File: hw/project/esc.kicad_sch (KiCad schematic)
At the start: 0 parts

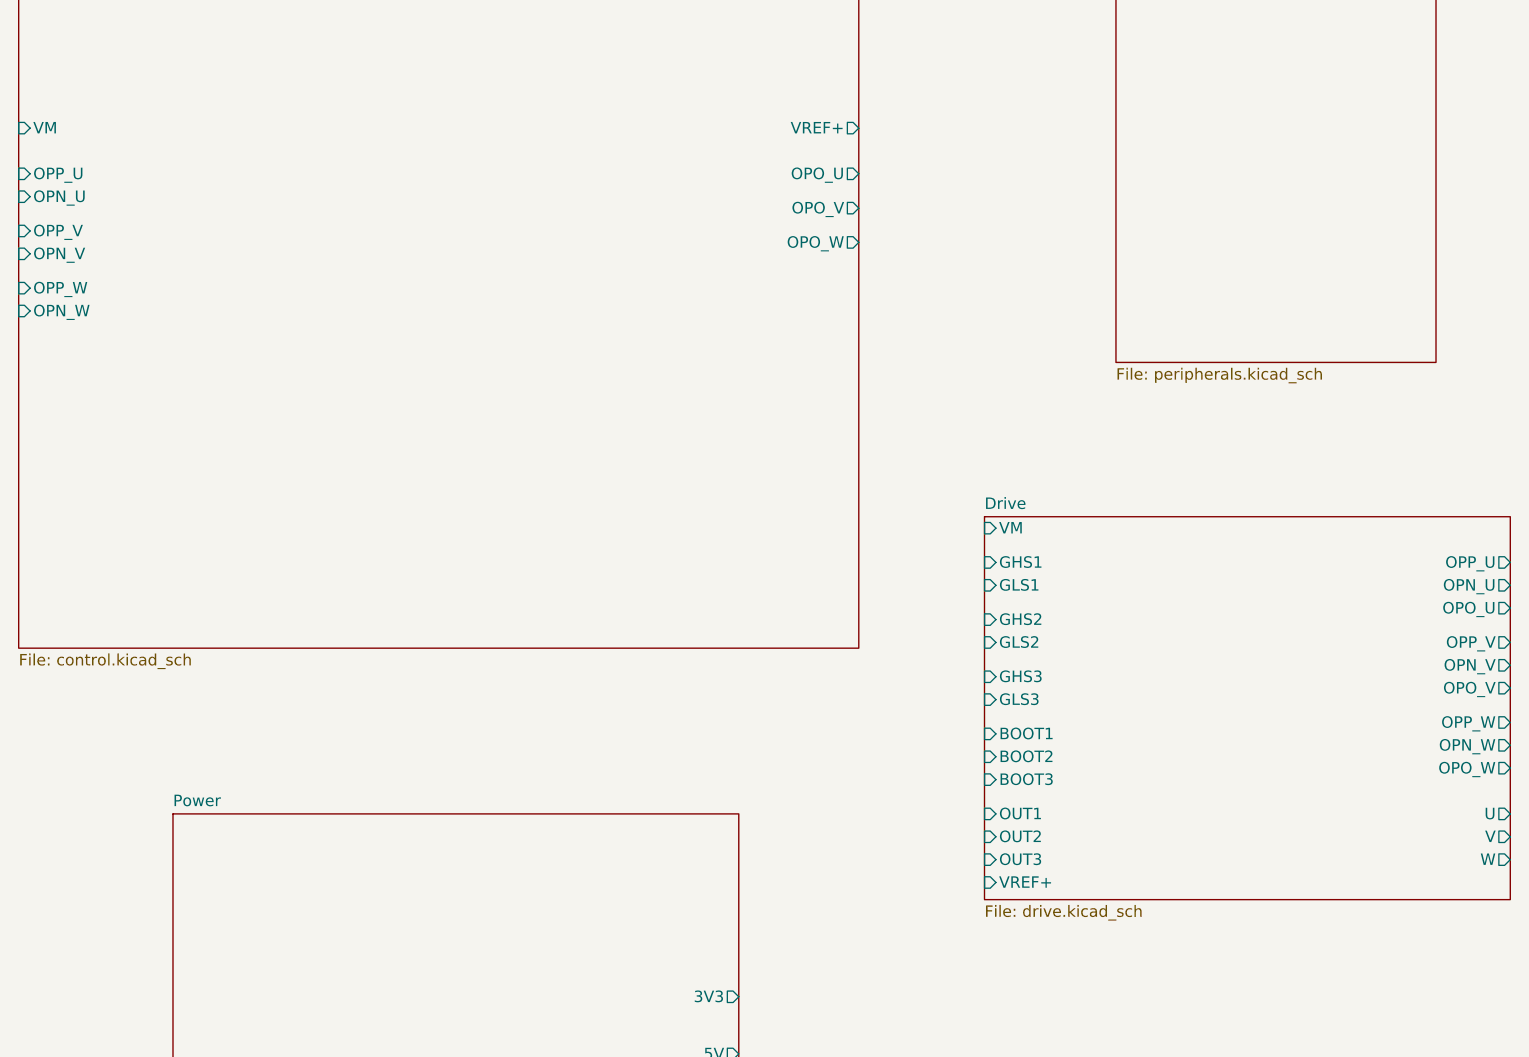
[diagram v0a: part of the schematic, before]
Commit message: Remove VINP and VOUT pins, updated pin functions on VINM pins
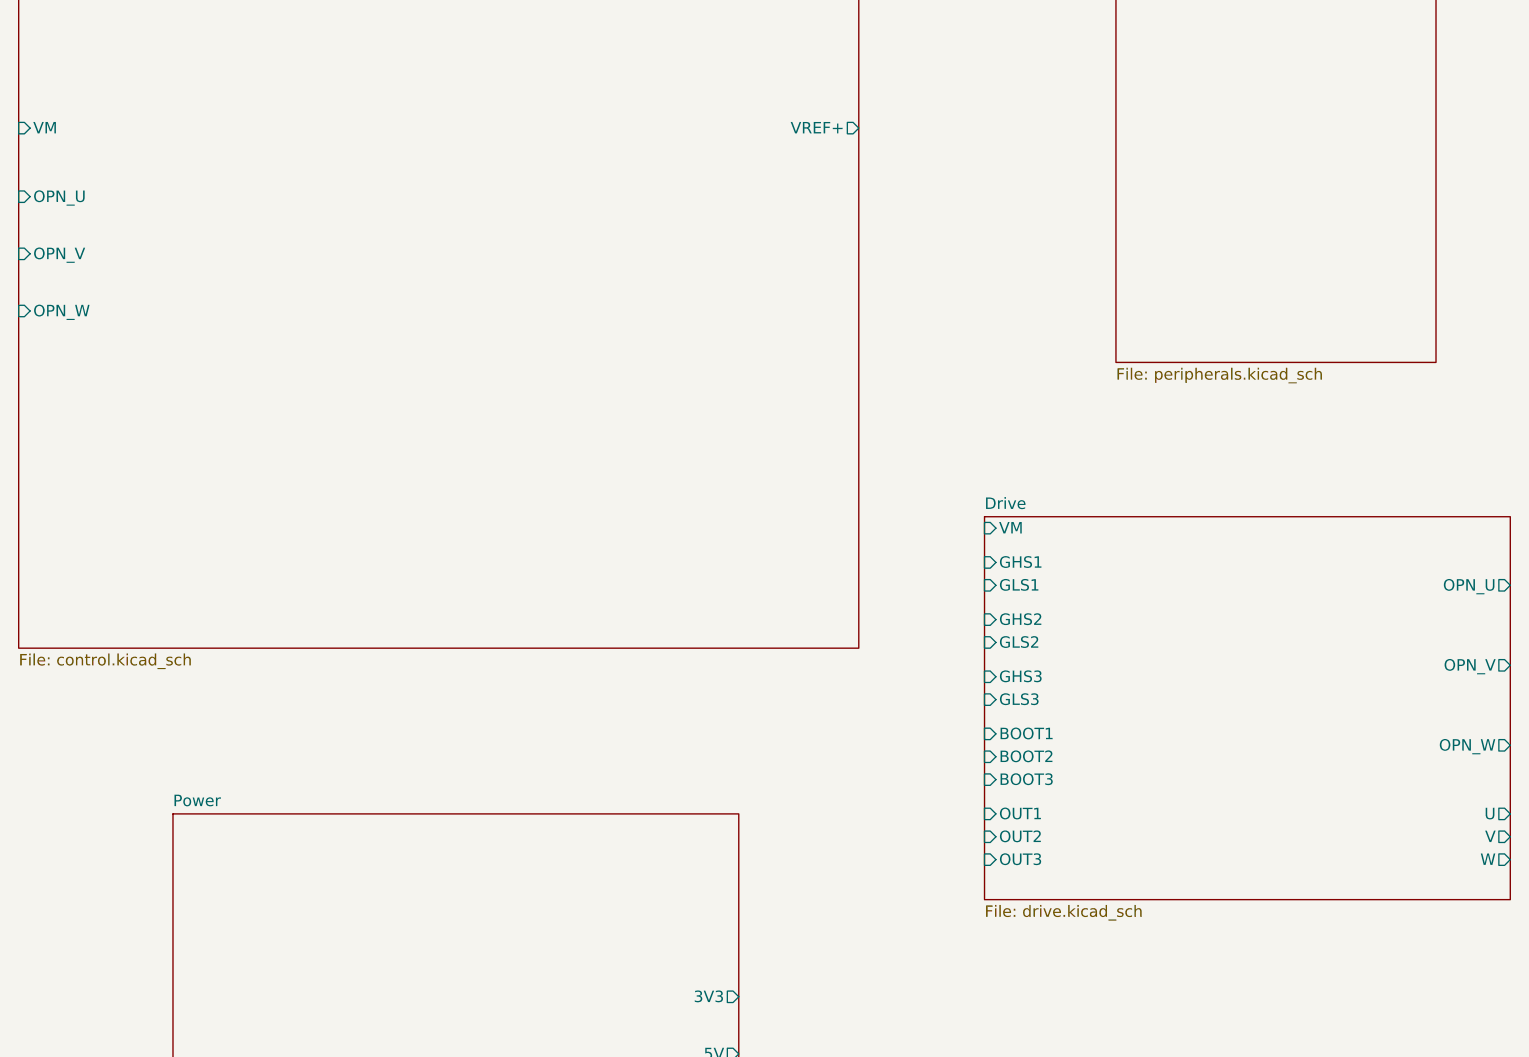
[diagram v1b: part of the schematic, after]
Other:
- sheet Control ports: added none; removed OPO_U, OPO_V, OPO_W, OPP_U, OPP_V, OPP_W
- sheet Drive ports: added none; removed OPO_U, OPO_V, OPO_W, OPP_U, OPP_V, OPP_W, VREF+
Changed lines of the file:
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@@
-			)
-		)
-		(pin "OPO_U" output
-			(at 106.68 44.45 0)
-			(effects
-				(font
-					(size 1.27 1.27)
-				)
-				(justify right)
-			)
-		)
-		(pin "OPO_V" output
-			(at 106.68 48.26 0)
-			(effects
-				(font
-					(size 1.27 1.27)
-				)
-				(justify right)
-			)
-		)
-		(pin "OPO_W" output
-			(at 106.68 52.07 0)
-			(effects
-				(font
-					(size 1.27 1.27)
-				)
-				(justify right)
-			)
-		)
-		(pin "OPP_U" input
-			(at 13.335 44.45 180)
-			(effects
-				(font
-					(size 1.27 1.27)
-				)
-				(justify left)
-			)
-		)
-		(pin "OPP_V" input
-			(at 13.335 50.8 180)
-			(effects
-				(font
-					(size 1.27 1.27)
-				)
-				(justify left)
-			)
-		)
-		(pin "OPP_W" input
-			(at 13.335 57.15 180)
-			(effects
-				(font
-					(size 1.27 1.27)
-				)
-				(justify left)
 			)
 		)
@@
 			)
 		)
-		(pin "VREF+" input
-			(at 120.65 123.19 180)
-			(effects
-				(font
-					(size 1.27 1.27)
-				)
-				(justify left)
-			)
-		)
-		(pin "OPP_V" output
-			(at 179.07 96.52 0)
-			(effects
-				(font
-					(size 1.27 1.27)
-				)
-				(justify right)
-			)
-		)
-		(pin "OPO_W" output
-			(at 179.07 110.49 0)
-			(effects
-				(font
-					(size 1.27 1.27)
-				)
-				(justify right)
-			)
-		)
-		(pin "OPP_U" output
-			(at 179.07 87.63 0)
-			(effects
-				(font
-					(size 1.27 1.27)
-				)
-				(justify right)
-			)
-		)
 		(pin "OPN_U" output
 			(at 179.07 90.17 0)
@@
 			)
 		)
-		(pin "OPP_W" output
-			(at 179.07 105.41 0)
-			(effects
-				(font
-					(size 1.27 1.27)
-				)
-				(justify right)
-			)
-		)
 		(pin "OPN_W" output
 			(at 179.07 107.95 0)
@@
 			)
 		)
-		(pin "OPO_V" output
-			(at 179.07 101.6 0)
-			(effects
-				(font
-					(size 1.27 1.27)
-				)
-				(justify right)
-			)
-		)
 		(pin "OPN_V" output
 			(at 179.07 99.06 0)
 			(effects
 				(font
-					(size 1.27 1.27)
-				)
-				(justify right)
-			)
-		)
-		(pin "OPO_U" output
-			(at 179.07 92.71 0)
-			(effects
-				(font

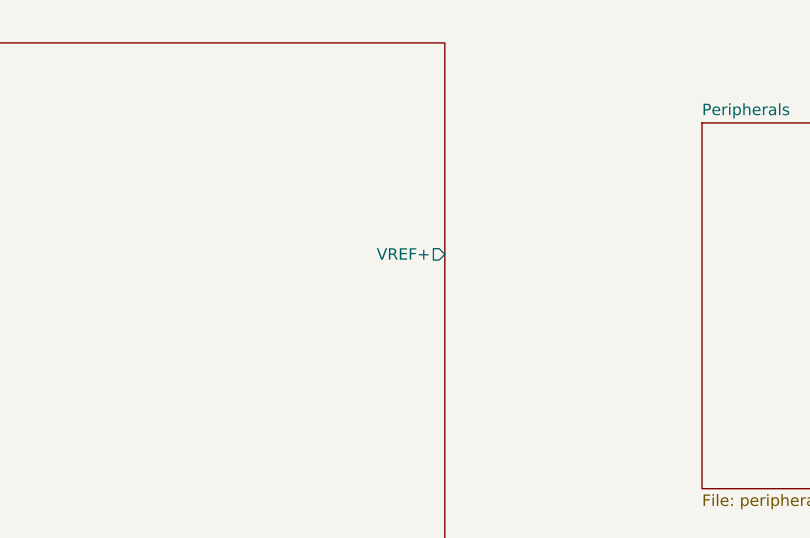
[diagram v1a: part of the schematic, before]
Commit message: Remove VREF+ as hierarchical label cuz PGA used now
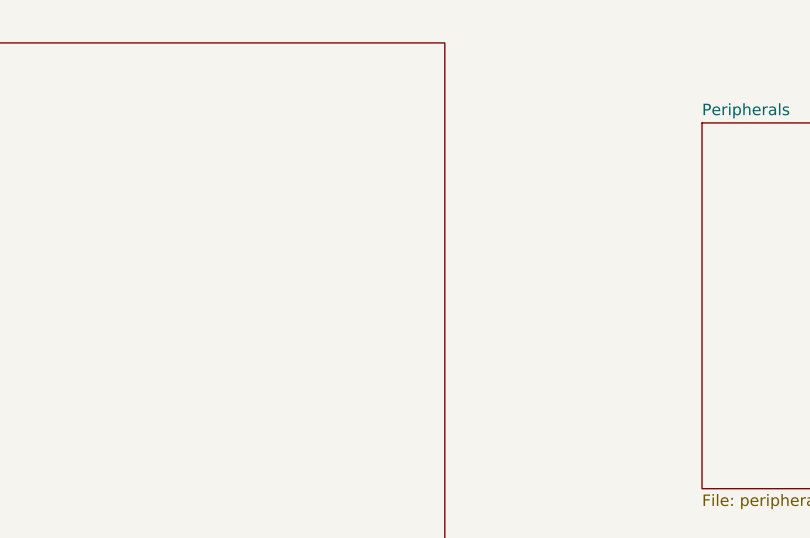
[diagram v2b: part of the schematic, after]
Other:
- sheet Control ports: added none; removed VREF+
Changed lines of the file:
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@@
-			)
-		)
-		(pin "VREF+" output
-			(at 106.68 39.37 0)
-			(effects
-				(font
-					(size 1.27 1.27)
-				)
-				(justify right)
 			)
 		)

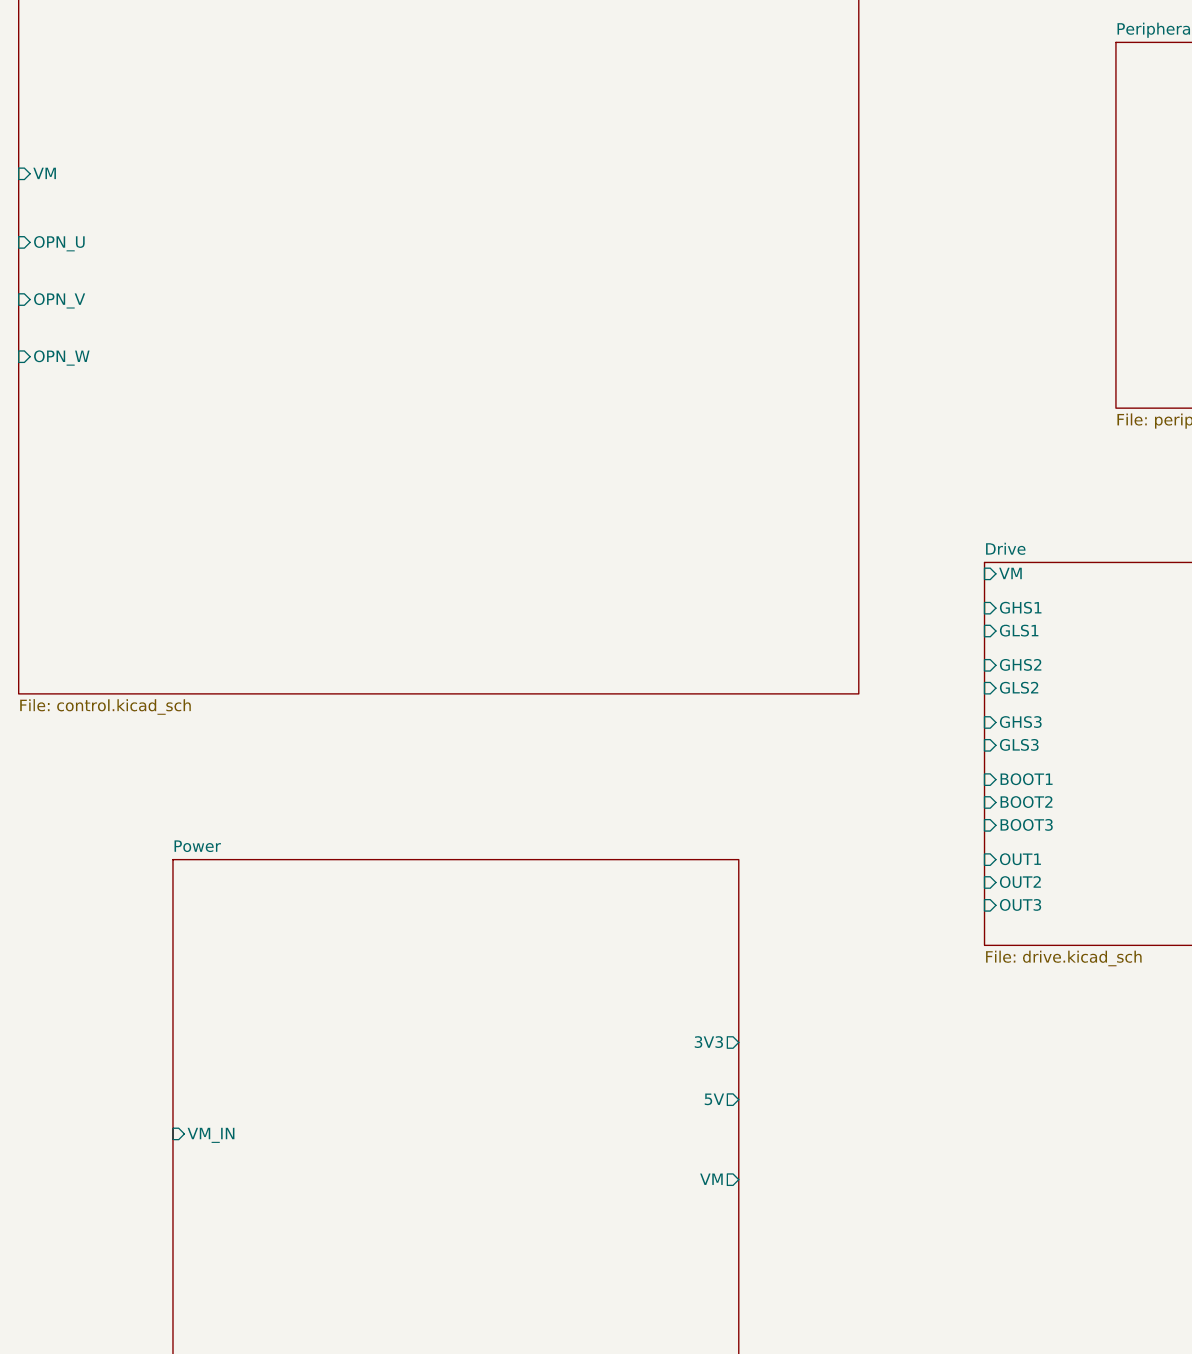
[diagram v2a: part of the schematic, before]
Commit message: Change VM to global source
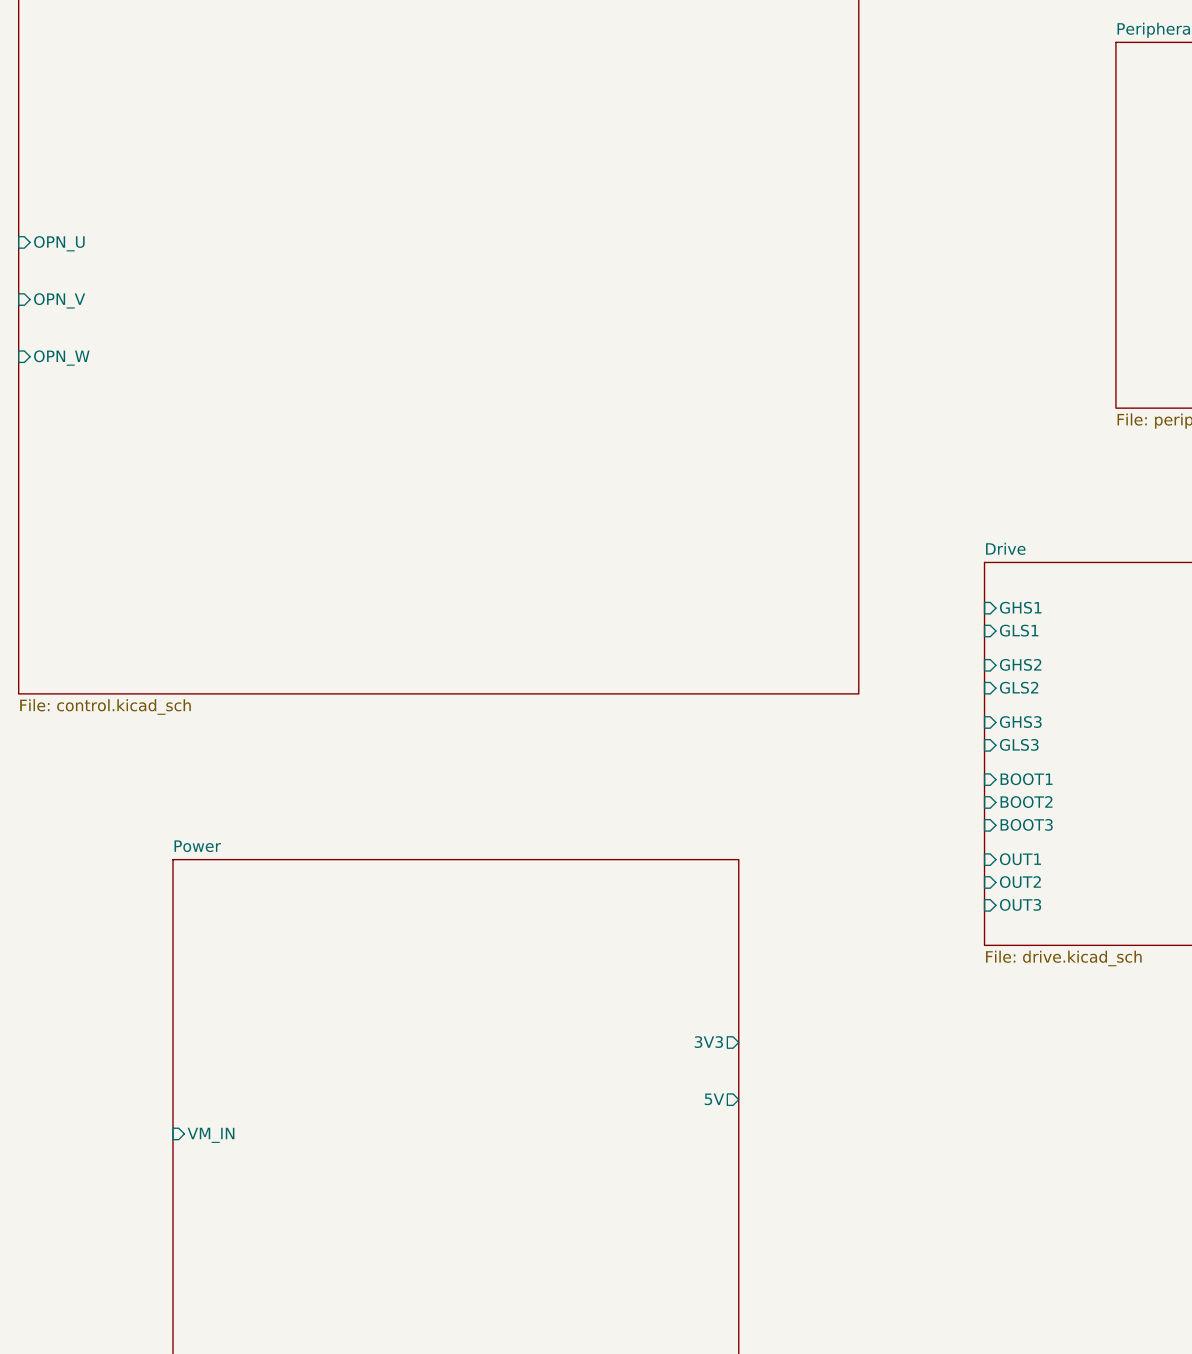
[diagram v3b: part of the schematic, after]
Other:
- sheet Control ports: added none; removed VM
- sheet Drive ports: added none; removed VM
- sheet Power ports: added none; removed VM
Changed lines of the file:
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@@
-			)
-		)
-		(pin "VM" input
-			(at 13.335 39.37 180)
-			(effects
-				(font
-					(size 1.27 1.27)
-				)
-				(justify left)
 			)
 		)
@@
 			)
 		)
-		(pin "VM" output
-			(at 93.345 151.13 0)
-			(effects
-				(font
-					(size 1.27 1.27)
-				)
-				(justify right)
-			)
-		)
 		(pin "VM_IN" input
 			(at 30.48 146.05 180)
@@
 			(effects
 				(font
-					(size 1.27 1.27)
-				)
-				(justify left)
-			)
-		)
-		(pin "VM" input
-			(at 120.65 83.82 180)
-			(effects
-				(font

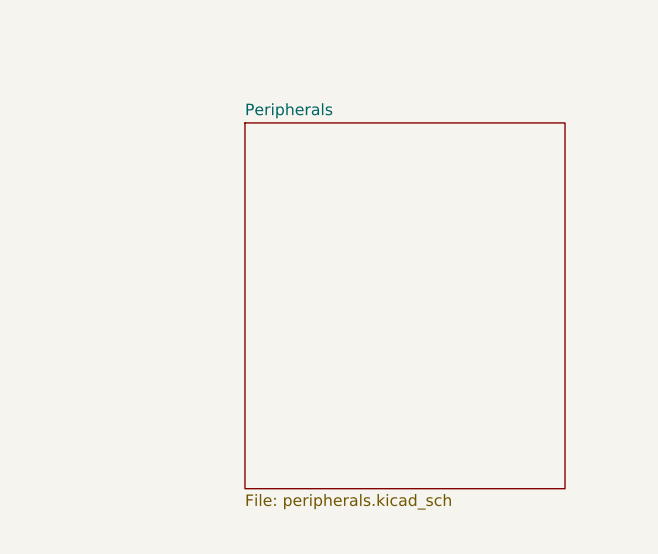
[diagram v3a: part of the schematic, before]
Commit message: Update root sheet with periph H labels, excluding LED signals
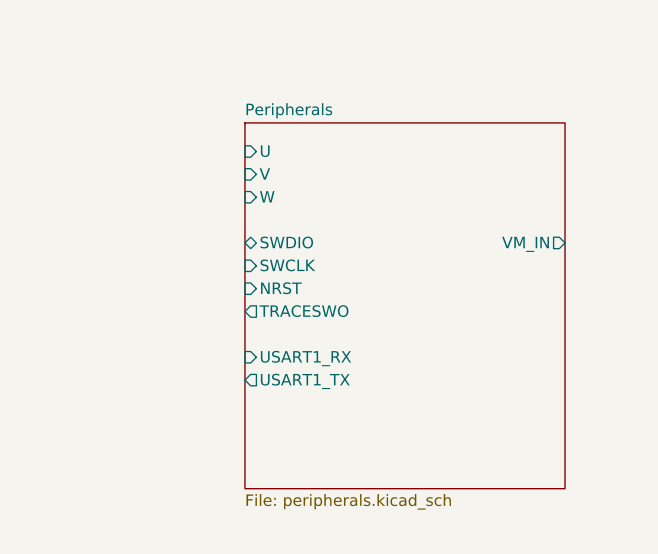
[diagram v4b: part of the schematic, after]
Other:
- sheet Peripherals ports: added NRST, SWCLK, SWDIO, TRACESWO, U, USART1_RX, USART1_TX, V, VM_IN, W; removed none
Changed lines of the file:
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@@
+			)
+		)
+		(pin "NRST" input
+			(at 135.255 43.18 180)
+			(effects
+				(font
+					(size 1.27 1.27)
+				)
+				(justify left)
+			)
+		)
+		(pin "SWCLK" input
+			(at 135.255 40.64 180)
+			(effects
+				(font
+					(size 1.27 1.27)
+				)
+				(justify left)
+			)
+		)
+		(pin "SWDIO" bidirectional
+			(at 135.255 38.1 180)
+			(effects
+				(font
+					(size 1.27 1.27)
+				)
+				(justify left)
+			)
+		)
+		(pin "TRACESWO" output
+			(at 135.255 45.72 180)
+			(effects
+				(font
+					(size 1.27 1.27)
+				)
+				(justify left)
+			)
+		)
+		(pin "U" input
+			(at 135.255 27.94 180)
+			(effects
+				(font
+					(size 1.27 1.27)
+				)
+				(justify left)
+			)
+		)
+		(pin "USART1_RX" input
+			(at 135.255 50.8 180)
+			(effects
+				(font
+					(size 1.27 1.27)
+				)
+				(justify left)
+			)
+		)
+		(pin "USART1_TX" output
+			(at 135.255 53.34 180)
+			(effects
+				(font
+					(size 1.27 1.27)
+				)
+				(justify left)
+			)
+		)
+		(pin "V" input
+			(at 135.255 30.48 180)
+			(effects
+				(font
+					(size 1.27 1.27)
+				)
+				(justify left)
+			)
+		)
+		(pin "VM_IN" output
+			(at 170.815 38.1 0)
+			(effects
+				(font
+					(size 1.27 1.27)
+				)
+				(justify right)
+			)
+		)
+		(pin "W" input
+			(at 135.255 33.02 180)
+			(effects
+				(font
+					(size 1.27 1.27)
+				)
+				(justify left)
 			)
 		)
